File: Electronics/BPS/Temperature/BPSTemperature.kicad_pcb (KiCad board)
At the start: 2 copper layers, 75 x 65 mm, 59 parts, among them J1 Conn_02x10_Counter_Clockwise, J2 Logic Analyzer, J3 Conn_02x06_Counter_Clockwise, J4 Conn_02x06_Counter_Clockwise, SW1 SW_DIP_x06, U1 LTC2983

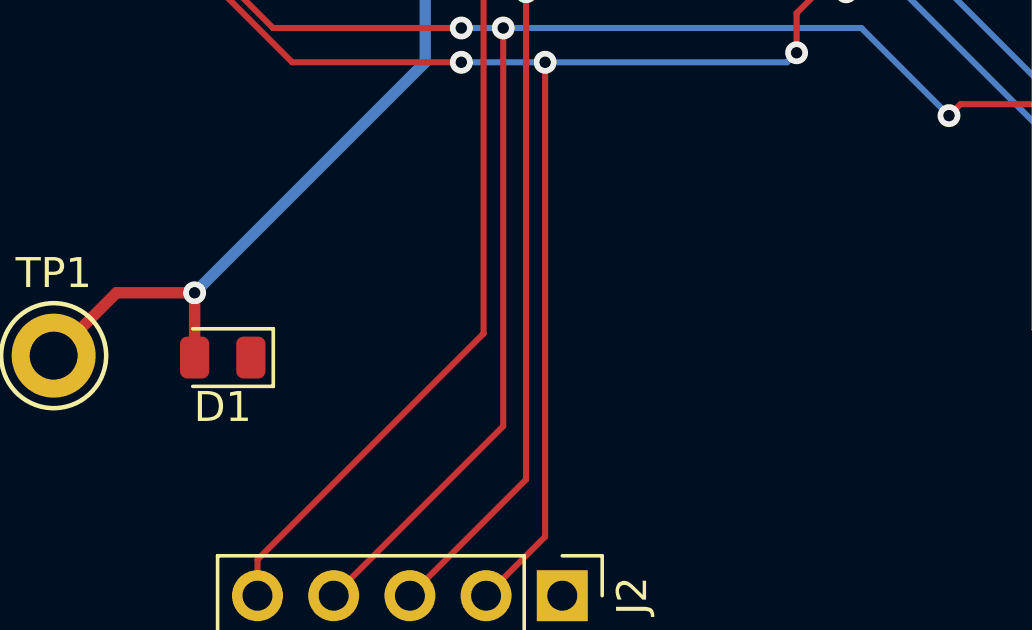
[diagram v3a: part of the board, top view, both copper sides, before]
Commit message: Completed PCB of Temperature Board for BPS
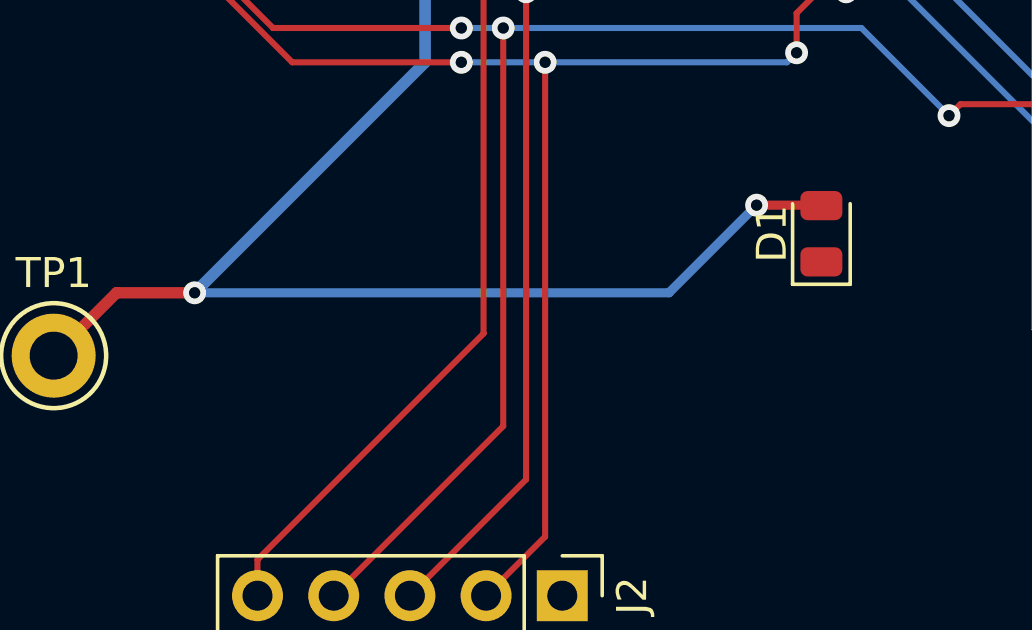
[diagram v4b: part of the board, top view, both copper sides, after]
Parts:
- moved D1 20.4 mm to (109.0, 117.6), turned to 90 degrees
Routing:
- net +5V: track 133.6 -> 153.5 mm, vias 3 -> 4
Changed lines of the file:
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@@
     (thickness 1.6)
     (drawings 4)
-    (tracks 589)
+    (tracks 593)
     (zones 0)
     (modules 59)
@@
       (effects (font (size 0.5 0.5) (thickness 0.08)))
     )
-    (pad 1 smd roundrect (at -0.9375 0 315) (size 0.975 1.4) (layers F.Cu F.Paste F.Mask) (roundrect_rratio 0.25)
+    (pad 1 smd roundrect (at -0.937501 0 315) (size 0.975 1.4) (layers F.Cu F.Paste F.Mask) (roundrect_rratio 0.25)
       (net 23 "Net-(C22-Pad1)"))
-    (pad 2 smd roundrect (at 0.9375 0 315) (size 0.975 1.4) (layers F.Cu F.Paste F.Mask) (roundrect_rratio 0.25)
+    (pad 2 smd roundrect (at 0.937501 0 315) (size 0.975 1.4) (layers F.Cu F.Paste F.Mask) (roundrect_rratio 0.25)
       (net 24 "Net-(C22-Pad2)"))
     (model ${KISYS3DMOD}/Capacitor_SMD.3dshapes/C_0805_2012Metric.wrl
@@
     (fp_line (start -1 -0.6) (end 1 -0.6) (layer F.Fab) (width 0.1))
     (fp_line (start -1 0.6) (end -1 -0.6) (layer F.Fab) (width 0.1))
-    (pad 2 smd roundrect (at 0.9375 0 225) (size 0.975 1.4) (layers F.Cu F.Paste F.Mask) (roundrect_rratio 0.25)
-      (net 1 GND))
-    (pad 1 smd roundrect (at -0.9375 0 225) (size 0.975 1.4) (layers F.Cu F.Paste F.Mask) (roundrect_rratio 0.25)
+    (pad 2 smd roundrect (at 0.937501 0 225) (size 0.975 1.4) (layers F.Cu F.Paste F.Mask) (roundrect_rratio 0.25)
+      (net 1 GND))
+    (pad 1 smd roundrect (at -0.937501 0 225) (size 0.975 1.4) (layers F.Cu F.Paste F.Mask) (roundrect_rratio 0.25)
       (net 25 "Net-(C23-Pad1)"))
     (model ${KISYS3DMOD}/Capacitor_SMD.3dshapes/C_0805_2012Metric.wrl
@@
     (fp_line (start -1 -0.6) (end 1 -0.6) (layer F.Fab) (width 0.1))
     (fp_line (start -1 0.6) (end -1 -0.6) (layer F.Fab) (width 0.1))
-    (pad 2 smd roundrect (at 0.9375 0 225) (size 0.975 1.4) (layers F.Cu F.Paste F.Mask) (roundrect_rratio 0.25)
-      (net 1 GND))
-    (pad 1 smd roundrect (at -0.9375 0 225) (size 0.975 1.4) (layers F.Cu F.Paste F.Mask) (roundrect_rratio 0.25)
+    (pad 2 smd roundrect (at 0.937501 0 225) (size 0.975 1.4) (layers F.Cu F.Paste F.Mask) (roundrect_rratio 0.25)
+      (net 1 GND))
+    (pad 1 smd roundrect (at -0.937501 0 225) (size 0.975 1.4) (layers F.Cu F.Paste F.Mask) (roundrect_rratio 0.25)
       (net 26 "Net-(C24-Pad1)"))
     (model ${KISYS3DMOD}/Capacitor_SMD.3dshapes/C_0805_2012Metric.wrl
@@
   )
   (module LED_SMD:LED_0805_2012Metric (layer F.Cu)
-    (at 89.0755 121.7295 180)
+    (at 109.0295 117.602 90)
     (descr "LED SMD 0805 (2012 Metric), square (rectangular) end terminal, IPC_7351 nominal, (Body size source: https://docs.google.com/spreadsheets/d/1BsfQQcO9C6DZCsRaXUlFlo91Tg2WpOkGARC1WS5S8t0/edit?usp=sharing), generated with kicad-footprint-generator")
     (tags diode)
     (attr smd)
-    (fp_text reference D1 (at 0 -1.65 180) (layer F.SilkS)
-      (effects (font (size 1 1) (thickness 0.15)))
-    )
-    (fp_text value LED (at 0 1.65 180) (layer F.Fab)
+    (fp_text reference D1 (at 0 -1.65 90) (layer F.SilkS)
+      (effects (font (size 1 1) (thickness 0.15)))
+    )
+    (fp_text value LED (at 0 1.65 90) (layer F.Fab)
       (effects (font (size 1 1) (thickness 0.15)))
     )
@@
     (fp_line (start 1.68 -0.95) (end 1.68 0.95) (layer F.CrtYd) (width 0.05))
     (fp_line (start 1.68 0.95) (end -1.68 0.95) (layer F.CrtYd) (width 0.05))
-    (fp_text user %R (at 0 0 180) (layer F.Fab)
+    (fp_text user %R (at 0 0 90) (layer F.Fab)
       (effects (font (size 0.5 0.5) (thickness 0.08)))
     )
-    (pad 1 smd roundrect (at -0.9375 0 180) (size 0.975 1.4) (layers F.Cu F.Paste F.Mask) (roundrect_rratio 0.25)
-      (net 1 GND))
-    (pad 2 smd roundrect (at 0.9375 0 180) (size 0.975 1.4) (layers F.Cu F.Paste F.Mask) (roundrect_rratio 0.25)
+    (pad 1 smd roundrect (at -0.9375 0 90) (size 0.975 1.4) (layers F.Cu F.Paste F.Mask) (roundrect_rratio 0.25)
+      (net 1 GND))
+    (pad 2 smd roundrect (at 0.9375 0 90) (size 0.975 1.4) (layers F.Cu F.Paste F.Mask) (roundrect_rratio 0.25)
       (net 22 +5V))
     (model ${KISYS3DMOD}/LED_SMD.3dshapes/LED_0805_2012Metric.wrl
@@
   (segment (start 95.8215 105.8545) (end 95.8215 111.887) (width 0.381) (layer B.Cu) (net 22))
   (segment (start 95.8215 111.887) (end 88.138 119.5705) (width 0.381) (layer B.Cu) (net 22))
-  (segment (start 88.138 119.5705) (end 88.138 121.7295) (width 0.381) (layer F.Cu) (net 22))
   (segment (start 85.5345 119.5705) (end 83.439 121.666) (width 0.381) (layer F.Cu) (net 22))
   (segment (start 88.138 119.5705) (end 85.5345 119.5705) (width 0.381) (layer F.Cu) (net 22))
@@
   (segment (start 88.773 93.9165) (end 89.535 93.9165) (width 0.381) (layer F.Cu) (net 22))
   (segment (start 89.535 93.9165) (end 92.202 93.9165) (width 0.381) (layer F.Cu) (net 22))
+  (via (at 106.8705 116.6495) (size 0.762) (drill 0.381) (layers F.Cu B.Cu) (net 22))
+  (segment (start 88.138 119.5705) (end 103.9495 119.5705) (width 0.3048) (layer B.Cu) (net 22))
+  (segment (start 103.9495 119.5705) (end 106.8705 116.6495) (width 0.3048) (layer B.Cu) (net 22))
+  (segment (start 109.0145 116.6495) (end 109.0295 116.6645) (width 0.3048) (layer F.Cu) (net 22))
+  (segment (start 106.8705 116.6495) (end 109.0145 116.6495) (width 0.3048) (layer F.Cu) (net 22))
   (segment (start 90.444242 97.127087) (end 91.094587 97.127087) (width 0.2032) (layer F.Cu) (net 23))
   (segment (start 88.459458 99.111871) (end 90.444242 97.127087) (width 0.2032) (layer F.Cu) (net 23))

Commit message: Updated Design Rules for Temperature Board for BPS
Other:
- net class PowerMax: via_dia 0.508 -> 0.762; via_drill 0.254 -> 0.381
- net class SignalMax: via_dia 0.508 -> 0.762; via_drill 0.254 -> 0.381
- rule via_min_size: 0.508 -> 0.381
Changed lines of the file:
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@@
     (via_size 0.762)
     (via_drill 0.381)
-    (via_min_size 0.508)
+    (via_min_size 0.381)
     (via_min_drill 0.254)
     (uvia_size 0.3)
@@
     (clearance 0.1524)
     (trace_width 0.381)
-    (via_dia 0.508)
-    (via_drill 0.254)
+    (via_dia 0.762)
+    (via_drill 0.381)
     (uvia_dia 0.3)
     (uvia_drill 0.1)
@@
     (clearance 0.1524)
     (trace_width 0.3048)
-    (via_dia 0.508)
-    (via_drill 0.254)
+    (via_dia 0.762)
+    (via_drill 0.381)
     (uvia_dia 0.3)
     (uvia_drill 0.1)
@@
   (segment (start 119.9345 109.5375) (end 121.11 108.362) (width 0.2032) (layer F.Cu) (net 50))
   (segment (start 109.855 109.5375) (end 119.9345 109.5375) (width 0.2032) (layer F.Cu) (net 50))
-  (via (at 99.187 109.5375) (size 0.762) (drill 0.381) (layers F.Cu B.Cu) (net 50))
+  (via (at 99.187 109.5375) (size 0.762) (drill 0.381) (layers F.Cu B.Cu) (net 50) (status 1000000))
   (segment (start 99.187 125.7935) (end 99.187 109.5375) (width 0.2032) (layer F.Cu) (net 50))
   (segment (start 95.3135 129.667) (end 99.187 125.7935) (width 0.2032) (layer F.Cu) (net 50))

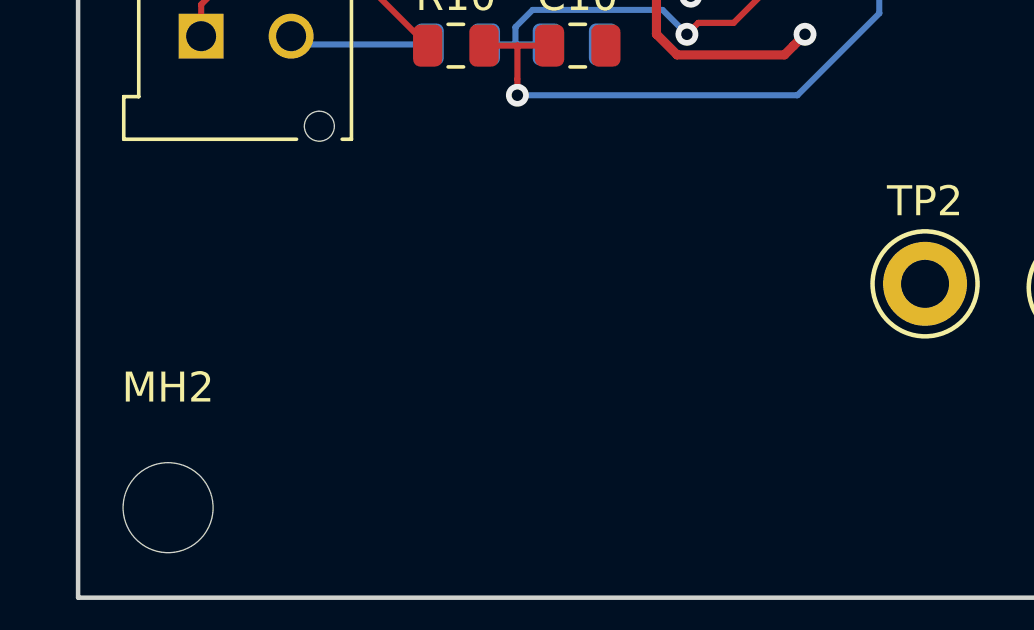
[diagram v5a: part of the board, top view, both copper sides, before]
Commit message: Added some Silk Screen Decals
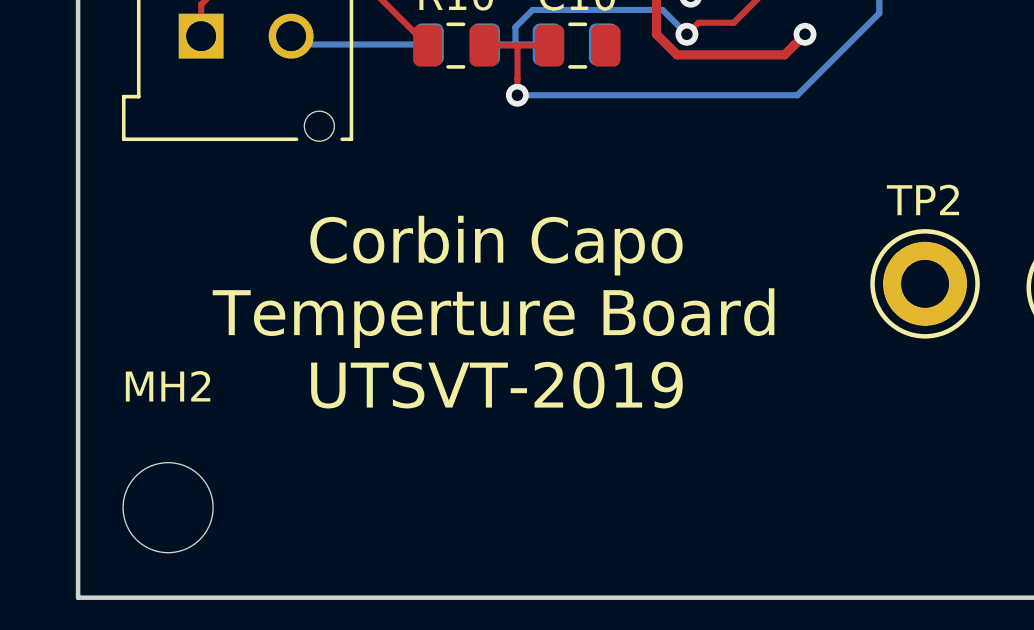
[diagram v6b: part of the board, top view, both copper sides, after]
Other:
- board text added: "Corbin Capo Temperture Board UTSVT-2019"
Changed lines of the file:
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@@
   (general
     (thickness 1.6)
-    (drawings 4)
+    (drawings 5)
     (tracks 593)
     (zones 0)
@@
     )
   )
+  (gr_text "Corbin Capo\nTemperture Board\nUTSVT-2019" (at 63.9445 122.555) (layer F.SilkS)
+    (effects (font (size 1.5 1.5) (thickness 0.3)))
+  )
   (gr_line (start 50 67) (end 50 132) (layer Edge.Cuts) (width 0.15))

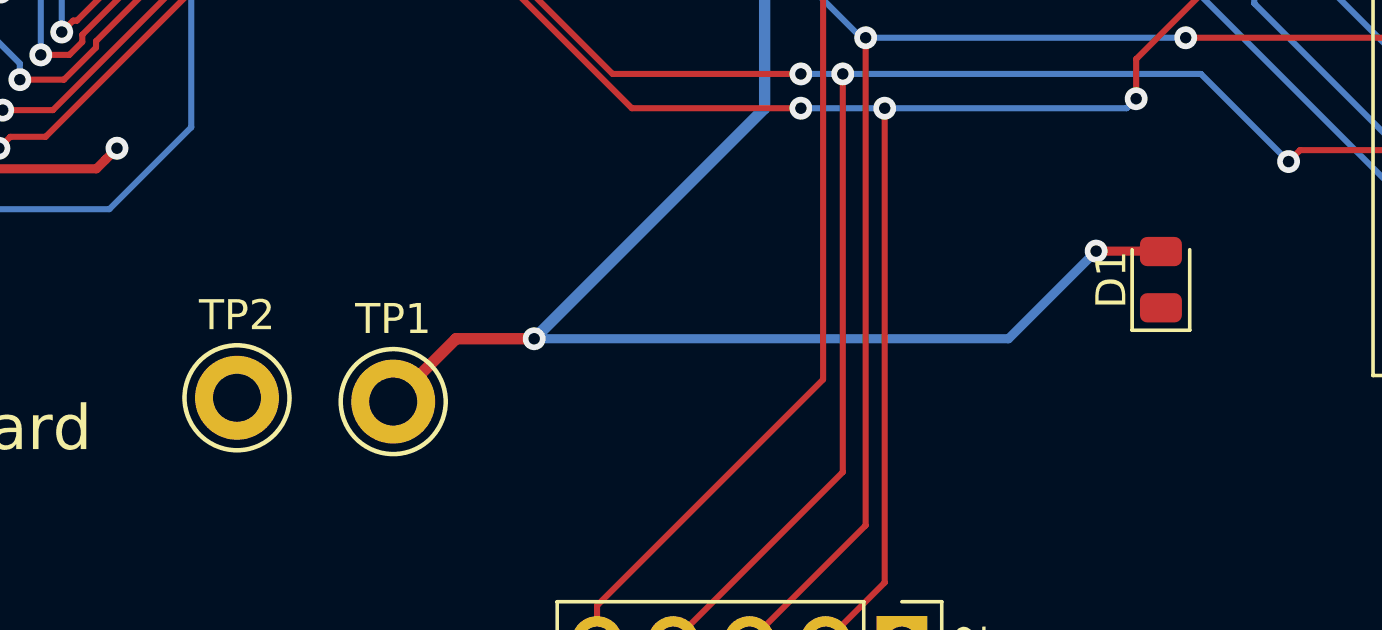
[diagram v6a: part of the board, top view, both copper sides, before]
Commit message: Added references to PCB of Temperture Board for BPS
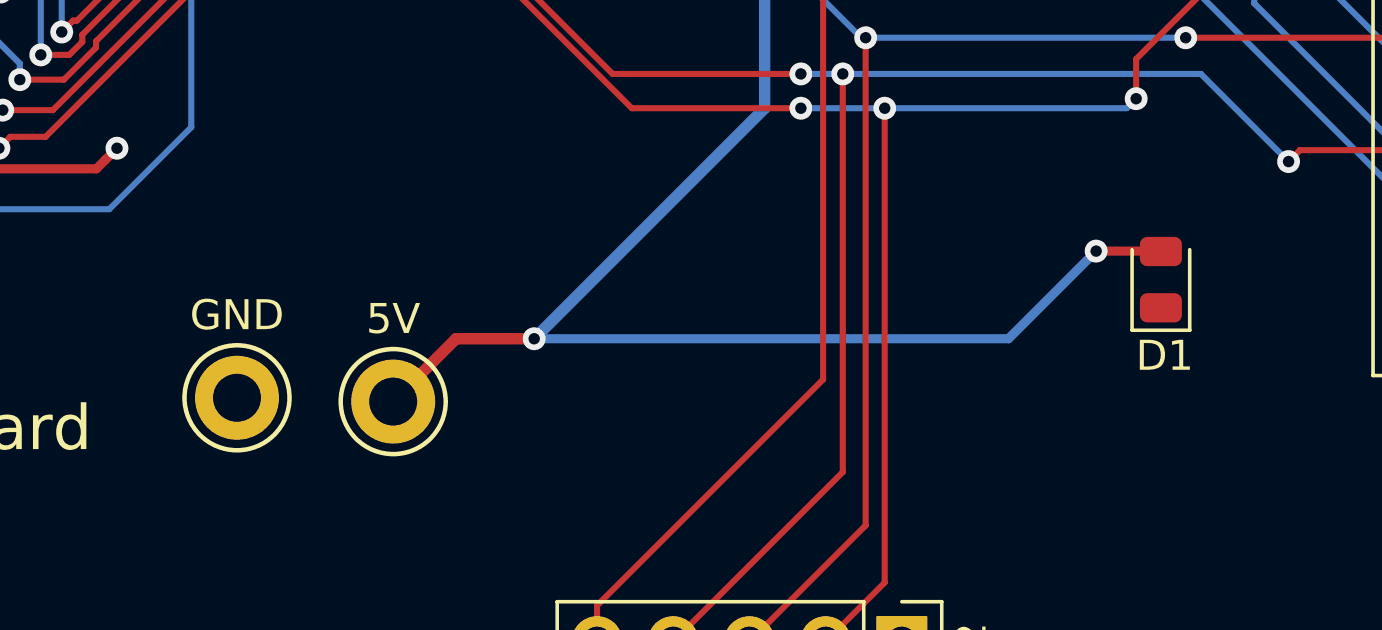
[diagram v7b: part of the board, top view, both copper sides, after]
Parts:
- renumbered TP1 to 5V, TP2 to GND
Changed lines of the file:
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@@
     (tags diode)
     (attr smd)
-    (fp_text reference D1 (at 0 -1.65 90) (layer F.SilkS)
+    (fp_text reference D1 (at -2.54 0.127 180) (layer F.SilkS)
       (effects (font (size 1 1) (thickness 0.15)))
     )
@@
     (descr "Keystone Miniature THM Test Point 5005-5009, http://www.keyelco.com/product-pdf.cfm?p=1314")
     (tags "Through Hole Mount Test Points")
-    (fp_text reference TP1 (at 0 -2.75) (layer F.SilkS)
+    (fp_text reference 5V (at 0 -2.75) (layer F.SilkS)
       (effects (font (size 1 1) (thickness 0.15)))
     )
@@
     (descr "Keystone Miniature THM Test Point 5005-5009, http://www.keyelco.com/product-pdf.cfm?p=1314")
     (tags "Through Hole Mount Test Points")
-    (fp_text reference TP2 (at 0 -2.75) (layer F.SilkS)
-      (effects (font (size 1 1) (thickness 0.15)))
-    )
+    (fp_text reference GND (at 0 -2.75) (layer F.SilkS)
+      (effects (font (size 1 1) (thickness 0.15)))
+    )
